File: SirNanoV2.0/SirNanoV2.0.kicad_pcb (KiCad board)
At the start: 2 copper layers, 45.2 x 18 mm, 43 parts, among them J1 Conn_01x14, J2 Conn_01x14, J3 USB_B_Micro, U1 ATmega328PB-MU, U2 AP7365-ADJ

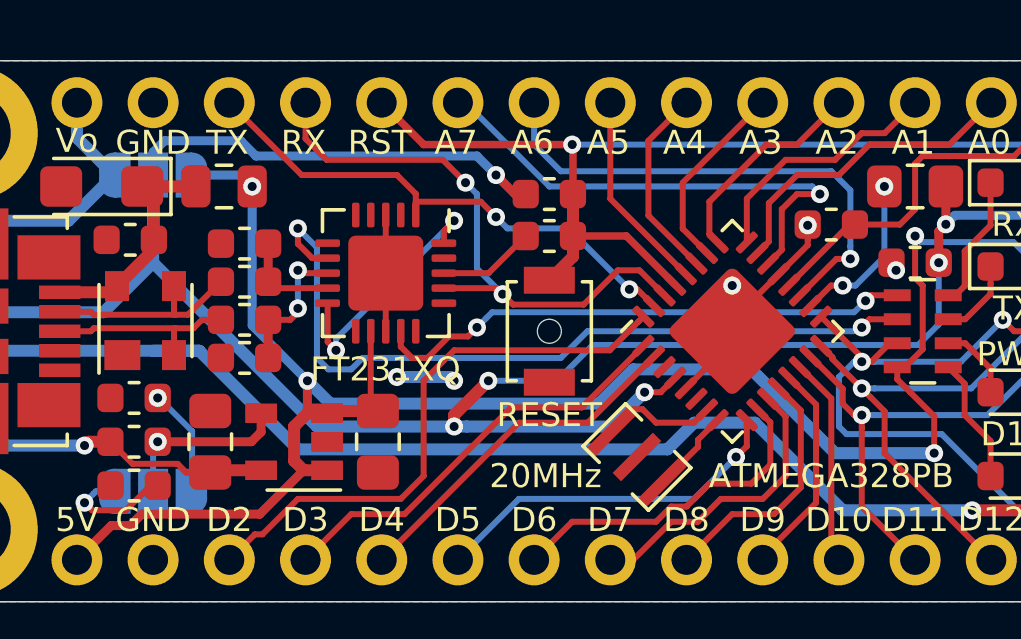
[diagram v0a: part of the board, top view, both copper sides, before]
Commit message: Fuse Footprint changed
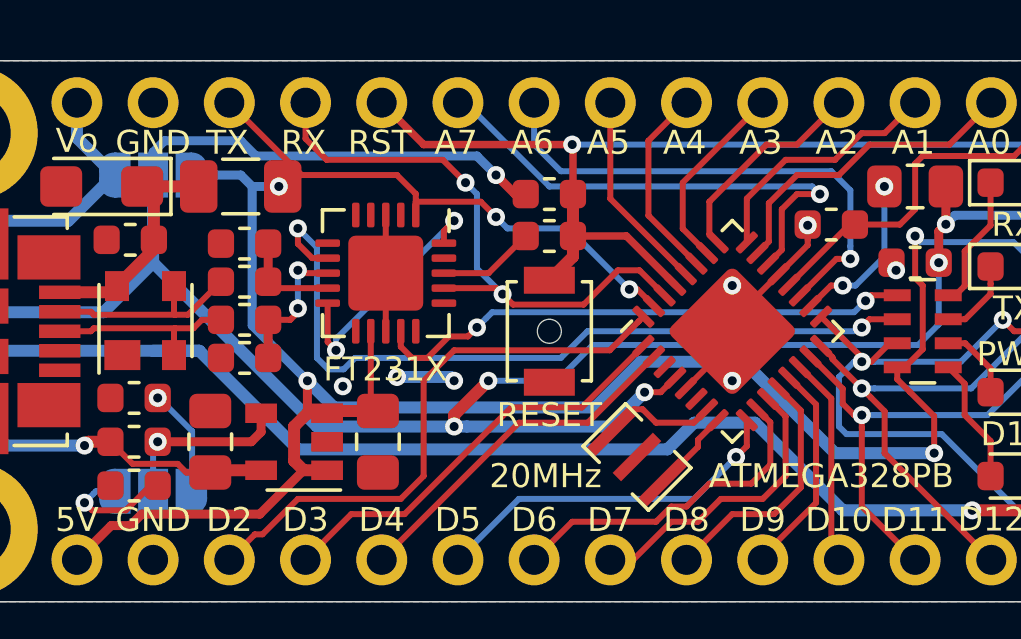
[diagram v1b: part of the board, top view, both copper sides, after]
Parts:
- C10, C9: value 2.2uF -> 1uF
- F1: footprint Resistor_SMD:R_0805_2012Metric -> Resistor_SMD:R_1206_3216Metric
- moved F1 0.56 mm to (117.7, 96.3)
- renumbered FT231XQ to FT231X
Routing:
- net 5V: track 65.9 -> 67.1 mm
- net GND: vias 6 -> 8
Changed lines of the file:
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@@
     (thickness 1.6)
     (drawings 60)
-    (tracks 464)
+    (tracks 467)
     (zones 0)
     (modules 43)
@@
   (layers
     (0 F.Cu signal)
-    (31 B.Cu signal hide)
+    (31 B.Cu signal)
     (32 B.Adhes user hide)
     (33 F.Adhes user hide)
@@
   )
   (setup
-    (last_trace_width 0.4)
+    (last_trace_width 0.3)
     (user_trace_width 0.127)
     (user_trace_width 0.15)
@@
     (add_net VOUT)
   )
+  (module Resistor_SMD:R_1206_3216Metric (layer F.Cu)
+    (at 117.729 96.266 180)
+    (descr "Resistor SMD 1206 (3216 Metric), square (rectangular) end terminal, IPC_7351 nominal, (Body size source: http://www.tortai-tech.com/upload/download/2011102023233369053.pdf), generated with kicad-footprint-generator")
+    (tags resistor)
+    (attr smd)
+    (fp_text reference F1 (at 0.0635 -0.0635 90) (layer F.SilkS) hide
+      (effects (font (size 0.7 0.7) (thickness 0.12)))
+    )
+    (fp_text value 500mA (at 0 1.65) (layer F.Fab)
+      (effects (font (size 1 1) (thickness 0.15)))
+    )
+    (fp_text user %R (at 0 0) (layer F.Fab)
+      (effects (font (size 0.5 0.5) (thickness 0.08)))
+    )
+    (fp_line (start 2.28 1.12) (end -2.28 1.12) (layer F.CrtYd) (width 0.05))
+    (fp_line (start 2.28 -1.12) (end 2.28 1.12) (layer F.CrtYd) (width 0.05))
+    (fp_line (start -2.28 -1.12) (end 2.28 -1.12) (layer F.CrtYd) (width 0.05))
+    (fp_line (start -2.28 1.12) (end -2.28 -1.12) (layer F.CrtYd) (width 0.05))
+    (fp_line (start -0.602064 0.91) (end 0.602064 0.91) (layer F.SilkS) (width 0.12))
+    (fp_line (start -0.602064 -0.91) (end 0.602064 -0.91) (layer F.SilkS) (width 0.12))
+    (fp_line (start 1.6 0.8) (end -1.6 0.8) (layer F.Fab) (width 0.1))
+    (fp_line (start 1.6 -0.8) (end 1.6 0.8) (layer F.Fab) (width 0.1))
+    (fp_line (start -1.6 -0.8) (end 1.6 -0.8) (layer F.Fab) (width 0.1))
+    (fp_line (start -1.6 0.8) (end -1.6 -0.8) (layer F.Fab) (width 0.1))
+    (pad 2 smd roundrect (at 1.4 0 180) (size 1.25 1.75) (layers F.Cu F.Paste F.Mask) (roundrect_rratio 0.2)
+      (net 54 VBUS))
+    (pad 1 smd roundrect (at -1.4 0 180) (size 1.25 1.75) (layers F.Cu F.Paste F.Mask) (roundrect_rratio 0.2)
+      (net 30 5V))
+    (model ${KISYS3DMOD}/Resistor_SMD.3dshapes/R_1206_3216Metric.wrl
+      (at (xyz 0 0 0))
+      (scale (xyz 1 1 1))
+      (rotate (xyz 0 0 0))
+    )
+  )
   (module Symbol:OSHW-Logo2_9.8x8mm_SilkScreen (layer B.Cu)
     (at 140.462 101.092 270)
@@
       (effects (font (size 0.8 0.8) (thickness 0.13)))
     )
-    (fp_text value 2.2uF (at 0 1.65 90) (layer F.Fab)
+    (fp_text value 1uF (at 0 1.65 90) (layer F.Fab)
       (effects (font (size 1 1) (thickness 0.15)))
     )
@@
     )
   )
-  (module Resistor_SMD:R_0805_2012Metric (layer F.Cu)
-    (at 117.1725 96.266 180)
-    (descr "Resistor SMD 0805 (2012 Metric), square (rectangular) end terminal, IPC_7351 nominal, (Body size source: https://docs.google.com/spreadsheets/d/1BsfQQcO9C6DZCsRaXUlFlo91Tg2WpOkGARC1WS5S8t0/edit?usp=sharing), generated with kicad-footprint-generator")
-    (tags resistor)
-    (attr smd)
-    (fp_text reference F1 (at 0.0635 -0.0635 90) (layer F.SilkS) hide
-      (effects (font (size 0.7 0.7) (thickness 0.12)))
-    )
-    (fp_text value 500mA (at 0 1.65) (layer F.Fab)
-      (effects (font (size 1 1) (thickness 0.15)))
-    )
-    (fp_line (start -1 0.6) (end -1 -0.6) (layer F.Fab) (width 0.1))
-    (fp_line (start -1 -0.6) (end 1 -0.6) (layer F.Fab) (width 0.1))
-    (fp_line (start 1 -0.6) (end 1 0.6) (layer F.Fab) (width 0.1))
-    (fp_line (start 1 0.6) (end -1 0.6) (layer F.Fab) (width 0.1))
-    (fp_line (start -0.258578 -0.71) (end 0.258578 -0.71) (layer F.SilkS) (width 0.12))
-    (fp_line (start -0.258578 0.71) (end 0.258578 0.71) (layer F.SilkS) (width 0.12))
-    (fp_line (start -1.68 0.95) (end -1.68 -0.95) (layer F.CrtYd) (width 0.05))
-    (fp_line (start -1.68 -0.95) (end 1.68 -0.95) (layer F.CrtYd) (width 0.05))
-    (fp_line (start 1.68 -0.95) (end 1.68 0.95) (layer F.CrtYd) (width 0.05))
-    (fp_line (start 1.68 0.95) (end -1.68 0.95) (layer F.CrtYd) (width 0.05))
-    (fp_text user %R (at 0 0) (layer F.Fab)
-      (effects (font (size 0.5 0.5) (thickness 0.08)))
-    )
-    (pad 1 smd roundrect (at -0.9375 0 180) (size 0.975 1.4) (layers F.Cu F.Paste F.Mask) (roundrect_rratio 0.25)
-      (net 30 5V))
-    (pad 2 smd roundrect (at 0.9375 0 180) (size 0.975 1.4) (layers F.Cu F.Paste F.Mask) (roundrect_rratio 0.25)
-      (net 54 VBUS))
-    (model ${KISYS3DMOD}/Resistor_SMD.3dshapes/R_0805_2012Metric.wrl
-      (at (xyz 0 0 0))
-      (scale (xyz 1 1 1))
-      (rotate (xyz 0 0 0))
-    )
-  )
   (module Capacitor_SMD:C_0805_2012Metric_Pad1.15x1.40mm_HandSolder (layer F.Cu)
     (at 116.713 104.775 90)
@@
       (effects (font (size 0.7 0.7) (thickness 0.12)))
     )
-    (fp_text value 2.2uF (at 0 1.65 90) (layer F.Fab)
+    (fp_text value 1uF (at 0 1.65 90) (layer F.Fab)
       (effects (font (size 1 1) (thickness 0.15)))
     )
@@
     (tags "QFN DFN_QFN")
     (attr smd)
-    (fp_text reference FT231XQ (at 3.2075 0.008) (layer F.SilkS)
+    (fp_text reference FT231X (at 3.2075 0.008) (layer F.SilkS)
       (effects (font (size 0.8 0.8) (thickness 0.13)))
     )
@@
   (via (at 139.573 99.06) (size 0.6) (drill 0.3) (layers F.Cu B.Cu) (net 1))
   (via (at 144.272 104.521) (size 0.6) (drill 0.3) (layers F.Cu B.Cu) (net 1))
+  (via (at 134.112 102.743) (size 0.6) (drill 0.3) (layers F.Cu B.Cu) (net 1))
+  (via (at 121.1326 102.92588) (size 0.6) (drill 0.3) (layers F.Cu B.Cu) (net 1))
   (via (at 137.795 99.568) (size 0.6) (drill 0.3) (layers F.Cu B.Cu) (net 3))
   (segment (start 137.403767 99.568) (end 137.795 99.568) (width 0.2) (layer F.Cu) (net 3))
@@
   (segment (start 129.286 101.092) (end 138.176 101.092) (width 0.2) (layer B.Cu) (net 10))
   (segment (start 128.397 101.981) (end 129.286 101.092) (width 0.2) (layer B.Cu) (net 10))
-  (segment (start 120.269 98.298) (end 120.269 101.981) (width 0.2) (layer B.Cu) (net 10))
+  (segment (start 121.539 101.981) (end 128.397 101.981) (width 0.2) (layer B.Cu) (net 10))
   (segment (start 119.634 97.663) (end 120.269 98.298) (width 0.2) (layer B.Cu) (net 10))
+  (segment (start 120.269 98.298) (end 120.269 101.981) (width 0.2) (layer B.Cu) (net 10))
   (segment (start 120.269 101.981) (end 120.65 102.362) (width 0.2) (layer B.Cu) (net 10))
-  (segment (start 120.65 102.362) (end 121.412 102.362) (width 0.2) (layer B.Cu) (net 10))
-  (segment (start 121.412 102.362) (end 121.793 101.981) (width 0.2) (layer B.Cu) (net 10))
-  (segment (start 121.793 101.981) (end 128.397 101.981) (width 0.2) (layer B.Cu) (net 10))
+  (segment (start 120.65 102.362) (end 121.158 102.362) (width 0.2) (layer B.Cu) (net 10))
+  (segment (start 121.158 102.362) (end 121.539 101.981) (width 0.2) (layer B.Cu) (net 10))
   (via (at 138.557 100.076) (size 0.6) (drill 0.3) (layers F.Cu B.Cu) (net 11))
   (segment (start 139.612 99.892) (end 138.741 99.892) (width 0.2) (layer F.Cu) (net 11))
@@
   (segment (start 122.063 103.512) (end 122.301 103.75) (width 0.2) (layer F.Cu) (net 30))
   (segment (start 122.063 101.092) (end 122.063 103.512) (width 0.2) (layer F.Cu) (net 30))
-  (via (at 118.11 96.266) (size 0.6) (drill 0.3) (layers F.Cu B.Cu) (net 30))
+  (via (at 118.999 96.266) (size 0.6) (drill 0.3) (layers F.Cu B.Cu) (net 30))
   (via (at 119.9515 102.743) (size 0.6) (drill 0.3) (layers F.Cu B.Cu) (net 30))
-  (segment (start 118.11 96.266) (end 118.11 100.9015) (width 0.3) (layer B.Cu) (net 30))
   (segment (start 118.11 100.9015) (end 119.9515 102.743) (width 0.3) (layer B.Cu) (net 30))
   (segment (start 119.9515 103.8225) (end 119.949 103.825) (width 0.3) (layer F.Cu) (net 30))
@@
   (segment (start 140.843 103.923) (end 140.843 105.156) (width 0.2) (layer F.Cu) (net 30))
   (via (at 140.843 105.156) (size 0.6) (drill 0.3) (layers F.Cu B.Cu) (net 30))
-  (segment (start 137.541 105.156) (end 140.843 105.156) (width 0.4) (layer B.Cu) (net 30))
-  (segment (start 134.747 102.362) (end 137.541 105.156) (width 0.4) (layer B.Cu) (net 30))
-  (segment (start 130.81 102.362) (end 134.747 102.362) (width 0.4) (layer B.Cu) (net 30))
-  (segment (start 129.667 103.505) (end 130.81 102.362) (width 0.4) (layer B.Cu) (net 30))
-  (segment (start 119.9515 102.743) (end 120.7135 103.505) (width 0.4) (layer B.Cu) (net 30))
-  (segment (start 120.7135 103.505) (end 129.667 103.505) (width 0.4) (layer B.Cu) (net 30))
   (segment (start 143.835888 98.471388) (end 144.2975 98.933) (width 0.2) (layer B.Cu) (net 30))
   (segment (start 143.4847 98.1202) (end 143.835888 98.471388) (width 0.2) (layer B.Cu) (net 30))
   (segment (start 140.208 97.917) (end 140.4112 98.1202) (width 0.2) (layer B.Cu) (net 30))
   (segment (start 140.4112 98.1202) (end 143.4847 98.1202) (width 0.2) (layer B.Cu) (net 30))
+  (segment (start 118.11 96.266) (end 118.999 96.266) (width 0.3) (layer B.Cu) (net 30))
+  (segment (start 118.11 96.266) (end 118.11 100.9015) (width 0.3) (layer B.Cu) (net 30))
+  (segment (start 119.9515 102.743) (end 120.8405 103.632) (width 0.4) (layer B.Cu) (net 30))
+  (segment (start 137.541 105.156) (end 140.843 105.156) (width 0.4) (layer B.Cu) (net 30))
+  (segment (start 134.493 102.108) (end 137.541 105.156) (width 0.4) (layer B.Cu) (net 30))
+  (segment (start 131.064 102.108) (end 134.493 102.108) (width 0.4) (layer B.Cu) (net 30))
+  (segment (start 129.54 103.632) (end 131.064 102.108) (width 0.4) (layer B.Cu) (net 30))
+  (segment (start 120.8405 103.632) (end 129.54 103.632) (width 0.4) (layer B.Cu) (net 30))
   (via (at 124.841 97.409) (size 0.6) (drill 0.3) (layers F.Cu B.Cu) (net 31))
   (segment (start 124.5005 98.1545) (end 124.5005 97.7495) (width 0.2) (layer F.Cu) (net 31))

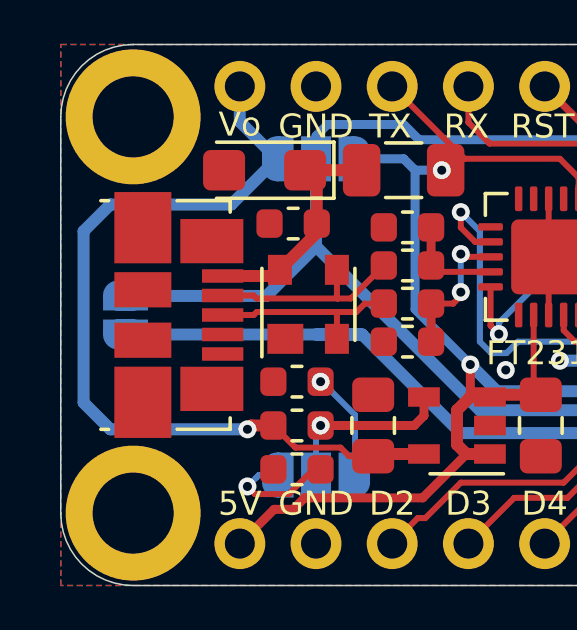
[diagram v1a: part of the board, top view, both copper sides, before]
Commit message: Silkscreen Edits
Dimensions moved to Drawings Layer
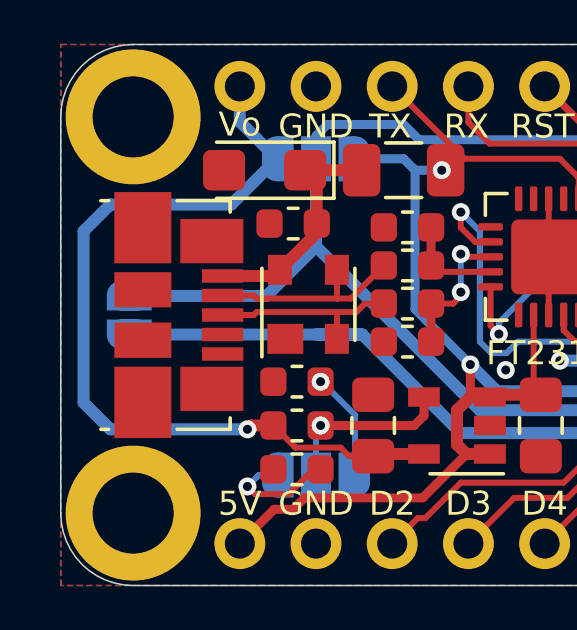
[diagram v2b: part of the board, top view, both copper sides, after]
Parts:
- moved JP1 0.13 mm to (108.6, 101.1)
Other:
- rule pad_to_mask_clearance: 0.051 -> 0
- rule solder_mask_min_width: 0.25 -> 0.1
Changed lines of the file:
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@@
     (34 B.Paste user hide)
     (35 F.Paste user hide)
-    (36 B.SilkS user hide)
+    (36 B.SilkS user)
     (37 F.SilkS user)
     (38 B.Mask user hide)
@@
   )
   (setup
-    (last_trace_width 0.3)
+    (last_trace_width 0.127)
     (user_trace_width 0.127)
     (user_trace_width 0.15)
@@
     (pad_size 0.8 1)
     (pad_drill 0)
-    (pad_to_mask_clearance 0.051)
-    (solder_mask_min_width 0.25)
+    (pad_to_mask_clearance 0)
+    (solder_mask_min_width 0.1)
     (aux_axis_origin 0 0)
     (visible_elements 7FFFFFFF)
     (pcbplotparams
-      (layerselection 0x010fc_ffffffff)
+      (layerselection 0x010f0_ffffffff)
       (usegerberextensions false)
       (usegerberattributes false)
@@
       (viasonmask false)
       (mode 1)
-      (useauxorigin false)
+      (useauxorigin true)
       (hpglpennumber 1)
       (hpglpenspeed 20)
@@
       (psa4output false)
       (plotreference true)
-      (plotvalue true)
+      (plotvalue false)
       (plotinvisibletext false)
       (padsonsilk false)
@@
       (outputformat 1)
       (mirror false)
-      (drillshape 1)
+      (drillshape 0)
       (scaleselection 1)
-      (outputdirectory ""))
+      (outputdirectory "../../Gerbers/SirNano/"))
   )
   (net 0 "")
@@
   )
   (module Jumper:SolderJumper-2_P1.3mm_Open_RoundedPad1.0x1.5mm (layer B.Cu)
-    (at 108.458 101.092 90)
+    (at 108.585 101.092 90)
     (descr "SMD Solder Jumper, 1x1.5mm, rounded Pads, 0.3mm gap, open")
     (tags "solder jumper open")
@@
     (descr "Through hole straight pin header, 1x14, 2.54mm pitch, single row")
     (tags "Through hole pin header THT 1x14 2.54mm single row")
-    (fp_text reference J1 (at 0 2.33 90) (layer B.SilkS)
+    (fp_text reference J1 (at 0 2.33 90) (layer B.SilkS) hide
       (effects (font (size 1 1) (thickness 0.15)) (justify mirror))
     )
@@
     )
   )
-  (gr_text Ext (at 108.458 103.632 90) (layer B.SilkS)
+  (gr_text Ext (at 108.585 103.505 90) (layer B.SilkS)
     (effects (font (size 0.8 0.8) (thickness 0.13)) (justify mirror))
   )
@@
     (effects (font (size 0.8 0.8) (thickness 0.13)) (justify mirror))
   )
-  (dimension 18.034 (width 0.12) (layer F.SilkS)
-    (gr_text "18.034 mm" (at 98.425 101.092 270) (layer F.SilkS)
+  (dimension 18.034 (width 0.12) (layer Dwgs.User)
+    (gr_text "18.034 mm" (at 98.425 101.092 270) (layer Dwgs.User)
       (effects (font (size 1 1) (thickness 0.15)) hide)
     )
@@
     (arrow2b (pts (xy 99.695 92.075) (xy 100.281421 93.201504)))
   )
-  (dimension 15.24 (width 0.12) (layer F.SilkS)
-    (gr_text "15.240 mm" (at 100.965 101.092 270) (layer F.SilkS)
+  (dimension 15.24 (width 0.12) (layer Dwgs.User)
+    (gr_text "15.240 mm" (at 100.965 101.092 270) (layer Dwgs.User)
       (effects (font (size 1 1) (thickness 0.15)) hide)
     )
@@
     (arrow2b (pts (xy 102.235 93.472) (xy 102.821421 94.598504)))
   )
-  (dimension 13.208 (width 0.12) (layer F.SilkS)
-    (gr_text "13.208 mm" (at 103.505 101.092 270) (layer F.SilkS)
+  (dimension 13.208 (width 0.12) (layer Dwgs.User)
+    (gr_text "13.208 mm" (at 103.505 101.092 270) (layer Dwgs.User)
       (effects (font (size 1 1) (thickness 0.15)) hide)
     )
@@
     (arrow2b (pts (xy 104.775 94.488) (xy 105.361421 95.614504)))
   )
-  (dimension 45.212 (width 0.12) (layer F.SilkS)
-    (gr_text "45.212 mm" (at 128.905 84.455) (layer F.SilkS)
+  (dimension 45.212 (width 0.12) (layer Dwgs.User)
+    (gr_text "45.212 mm" (at 128.905 84.455) (layer Dwgs.User)
       (effects (font (size 1 1) (thickness 0.15)) hide)
     )
@@
     (arrow2b (pts (xy 106.299 85.725) (xy 107.425504 85.138579)))
   )
-  (dimension 40.386 (width 0.12) (layer F.SilkS)
-    (gr_text "40.386 mm" (at 128.905 86.995) (layer F.SilkS)
+  (dimension 40.386 (width 0.12) (layer Dwgs.User)
+    (gr_text "40.386 mm" (at 128.905 86.995) (layer Dwgs.User)
       (effects (font (size 1 1) (thickness 0.15)) hide)
     )
@@
     (arrow2b (pts (xy 108.712 88.265) (xy 109.838504 87.678579)))
   )
-  (dimension 33.02 (width 0.12) (layer F.SilkS)
-    (gr_text "33.020 mm" (at 128.778 89.535) (layer F.SilkS)
+  (dimension 33.02 (width 0.12) (layer Dwgs.User)
+    (gr_text "33.020 mm" (at 128.778 89.535) (layer Dwgs.User)
       (effects (font (size 1 1) (thickness 0.15)) hide)
     )
@@
     (arrow2b (pts (xy 112.268 90.805) (xy 113.394504 90.218579)))
   )
-  (gr_text Aref (at 110.109 101.092 90) (layer B.SilkS)
+  (gr_text Aref (at 110.236 101.092 90) (layer B.SilkS)
     (effects (font (size 0.8 0.8) (thickness 0.13)) (justify mirror))
   )
-  (gr_text Vcc (at 108.331 98.552 90) (layer B.SilkS)
+  (gr_text Vcc (at 108.585 98.552 90) (layer B.SilkS)
     (effects (font (size 0.8 0.8) (thickness 0.13)) (justify mirror))
   )

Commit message: Page Settings Updated
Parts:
- moved ICSP6 85.0 mm to (88.0, 37.8)
- moved REF** 85.0 mm to (89.5, 47.0)
- moved 20MHz 85.0 mm to (71.4, 44.6)
- moved C10 85.0 mm to (57.1, 44.1)
- moved C2 85.0 mm to (58.3, 41.3)
- moved C4 85.0 mm to (58.3, 37.5)
- moved C6 85.0 mm to (54.5, 37.3)
- moved C7 85.0 mm to (80.6, 38.1)
- moved C8 85.0 mm to (53.5, 35.6)
- moved C9 85.0 mm to (62.7, 44.1)
- moved D1 85.0 mm to (55.0, 40.0)
- moved F1 85.0 mm to (58.2, 35.6)
- moved FT231X 85.0 mm to (63.0, 38.4)
- moved G*** 85.0 mm to (56.8, 40.4)
- moved G*** 85.0 mm to (74.7, 40.4)
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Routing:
- net VCC: track 76.2 -> 75.3 mm

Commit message: Part Numbers Added
Minor board Revisions
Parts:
- added C3: 100nF, Capacitor_SMD:C_0603_1608Metric, F.Cu at (62.3, 41.8)
- C10, C9: footprint Capacitor_SMD:C_0805_2012Metric_Pad1.15x1.40mm_HandSolder -> Capacitor_SMD:C_0603_1608Metric_Pad1.05x0.95mm_HandSolder
- RN1: footprint Resistor_SMD:R_Array_Concave_4x0603 -> Resistor_SMD:R_Array_Convex_4x0603
- moved R5 1.51 mm to (55.0, 44.1)
- moved R7 1.45 mm to (55.0, 42.7)
- renumbered FT231X to FT231XQ, D13 to IO13
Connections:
- FT231XQ pad 11: Net-(U3-Pad11) -> 3.3V
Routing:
- net VOUT: track 28.3 -> 37.5 mm, vias 1 -> 2
- net ADJ: track 5.92 -> 7.17 mm
- net 1.8V: track 3.61 -> 4.83 mm
- net 3.3V: track 8.52 -> 9.52 mm
- net TX_LED: track 26.4 -> 25.6 mm
